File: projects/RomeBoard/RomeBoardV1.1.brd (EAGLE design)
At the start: 110 x 135 mm, 27 parts, among them J1 HEADER-5, J2 RASPBERRY-PI-HEADER, M1 2N7000, M2 2N7000, M3 2N7000, U1 LM1084IT-ADJ

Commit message: fixing air wire + updating library
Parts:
- M1, M2, M3: value 2N7000 -> ZVN4424A
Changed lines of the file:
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@@
 <element name="R6" library="passives" package="AXIAL-0.4" value="147R" x="5" y="46" rot="R270"/>
 <element name="R7" library="passives" package="AXIAL-0.4" value="147R" x="32" y="34" rot="R270"/>
-<element name="M1" library="BrownSpaceEngineering" package="TO-923-MOS" value="2N7000" x="26" y="63" rot="R270"/>
-<element name="M2" library="BrownSpaceEngineering" package="TO-923-MOS" value="2N7000" x="12" y="51" rot="R270"/>
-<element name="M3" library="BrownSpaceEngineering" package="TO-923-MOS" value="2N7000" x="26" y="39" rot="R270"/>
+<element name="M1" library="BrownSpaceEngineering" package="TO-923-MOS" value="ZVN4424A" x="26" y="63" rot="R270"/>
+<element name="M2" library="BrownSpaceEngineering" package="TO-923-MOS" value="ZVN4424A" x="12" y="51" rot="R270"/>
+<element name="M3" library="BrownSpaceEngineering" package="TO-923-MOS" value="ZVN4424A" x="26" y="39" rot="R270"/>
 <element name="R8" library="passives" package="AXIAL-0.4" value="10K" x="105" y="78" rot="R270"/>
 <element name="U1" library="BrownSpaceEngineering" package="TO-220-507302B00000G" value="LM1084IT-ADJ" x="80" y="11.5" smashed="yes" rot="R90">
@@
 <vertex x="51.5" y="6" curve="90"/>
 <vertex x="52" y="6.5"/>
-<vertex x="52" y="14.5" curve="-90"/>
-<vertex x="52.5" y="15"/>
-<vertex x="67.5" y="15" curve="-90"/>
-<vertex x="68" y="14.5"/>
-<vertex x="68" y="10.5" curve="90"/>
-<vertex x="68.5" y="10"/>
+<vertex x="52" y="15" curve="-90"/>
+<vertex x="52.5" y="15.5"/>
+<vertex x="67.5" y="15.5" curve="-90"/>
+<vertex x="68.5" y="15"/>
+<vertex x="68.5" y="10.5" curve="90"/>
+<vertex x="69" y="10"/>
 <vertex x="82.5" y="10" curve="90"/>
 <vertex x="83" y="10.5"/>
@@
 <polygon width="0.254" layer="1" isolate="0.3048" thermals="no">
 <vertex x="94.5" y="21.5"/>
-<vertex x="94.5" y="19.5" curve="-90"/>
-<vertex x="94" y="19"/>
+<vertex x="94.5" y="21" curve="-90"/>
+<vertex x="92.5" y="19"/>
 <vertex x="77" y="19" curve="90"/>
 <vertex x="76.5" y="18.5"/>
@@
 <vertex x="84" y="14" curve="-90"/>
 <vertex x="84.5" y="14.5"/>
-<vertex x="96" y="14.5" curve="-90"/>
-<vertex x="96.5" y="14"/>
-<vertex x="96.5" y="11" curve="90"/>
-<vertex x="97" y="10.5"/>
-<vertex x="104" y="10.5" curve="90"/>
-<vertex x="104.5" y="11"/>
-<vertex x="104.5" y="17" curve="90"/>
-<vertex x="104" y="17.5"/>
-<vertex x="102" y="17.5" curve="-90"/>
-<vertex x="101.5" y="18"/>
+<vertex x="94" y="14.5" curve="-90"/>
+<vertex x="96.5" y="12.5"/>
+<vertex x="96.5" y="12" curve="90"/>
+<vertex x="98" y="10.5"/>
+<vertex x="103" y="10.5" curve="90"/>
+<vertex x="104.5" y="12"/>
+<vertex x="104.5" y="16.5" curve="90"/>
+<vertex x="103.5" y="17.5" curve="-90"/>
+<vertex x="101.5" y="20"/>
 <vertex x="101.5" y="21" curve="90"/>
 <vertex x="101" y="21.5"/>

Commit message: for review
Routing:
- net 3V6: track 13.1 -> 16.5 mm
- net RX_L: track 71.5 -> 70.9 mm
- net GND: track 2.51 -> 2.91 mm, vias 106 -> 110
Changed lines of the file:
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@@
 <element name="U1" library="BrownSpaceEngineering" package="TO-220-507302B00000G" value="LM1084IT-ADJ" x="80" y="11.5" smashed="yes" rot="R90">
 <attribute name="NAME" x="81.31" y="17.14" size="1.27" layer="25" rot="R180"/>
-<attribute name="VALUE" x="76.94" y="7.93" size="1.27" layer="27" rot="R90"/>
+<attribute name="VALUE" x="76.57" y="3.94" size="1.27" layer="27" rot="R180"/>
 </element>
 <element name="R2" library="passives" package="AXIAL-0.4" value="450R" x="43" y="4.5"/>
@@
 <wire x1="39.36" y1="43.19" x2="39.36" y2="41.86" width="0.254" layer="1"/>
 <wire x1="39.36" y1="41.86" x2="39" y2="41.5" width="0.254" layer="1"/>
-<wire x1="39.2894" y1="45.7606" x2="39.36" y2="45.69" width="0.254" layer="1"/>
 <wire x1="35.5" y1="47" x2="35.5700125" y2="47" width="0.254" layer="1"/>
 <wire x1="44.06" y1="45.19" x2="44.06" y2="45.69" width="0.254" layer="1"/>
@@
 <contactref element="C1" pad="-"/>
 <contactref element="C3" pad="-"/>
-<wire x1="39.36" y1="45.69" x2="39.36" y2="45.19" width="0" layer="19" extent="1-1"/>
+<wire x1="39.36" y1="45.69" x2="39.36" y2="45.19" width="0.254" layer="1"/>
+<via x="42" y="49.5" extent="1-16" drill="0.35"/>
+<via x="41.5" y="48.5" extent="1-16" drill="0.35"/>
+<via x="42" y="47.5" extent="1-16" drill="0.35"/>
+<via x="41.5" y="46.5" extent="1-16" drill="0.35"/>
 </signal>
 <signal name="3V6">
@@
 <wire x1="80" y1="11.5" x2="84.42" y2="11.5" width="1.27" layer="1"/>
 <wire x1="84.42" y1="11.5" x2="86" y2="13.08" width="1.27" layer="1"/>
-<wire x1="40.64513125" y1="46" x2="41" y2="46" width="0.254" layer="1"/>
 <wire x1="39.36" y1="46.19" x2="39.383" y2="46.167" width="0.254" layer="1"/>
 <wire x1="39.383" y1="46.167" x2="40.47813125" y2="46.167" width="0.254" layer="1"/>
-<wire x1="40.47813125" y1="46.167" x2="40.64513125" y2="46" width="0.254" layer="1"/>
 <wire x1="41" y1="44.5" x2="39.67" y2="44.5" width="0.254" layer="1"/>
-<wire x1="39.67" y1="44.5" x2="39.36" y2="44.19" width="0.254" layer="1"/>
-<wire x1="41" y1="46" x2="41" y2="44.5" width="0.254" layer="1"/>
+<wire x1="39.67" y1="44.5" x2="39.585" y2="44.415" width="0.254" layer="1"/>
+<wire x1="39.585" y1="44.415" x2="39.36" y2="44.19" width="0.254" layer="1"/>
 <polygon width="0.254" layer="1" isolate="0.3048" thermals="no">
 <vertex x="82.5" y="12.5"/>
@@
 <vertex x="83" y="12" curve="90"/>
 </polygon>
+<wire x1="39.36" y1="46.19" x2="37.69" y2="46.19" width="0.254" layer="1"/>
+<wire x1="37.69" y1="46.19" x2="37.5" y2="46" width="0.254" layer="1"/>
+<wire x1="37.5" y1="46" x2="37.5" y2="44.5" width="0.254" layer="1"/>
+<wire x1="37.5" y1="44.5" x2="39.5" y2="44.5" width="0.254" layer="1"/>
+<wire x1="39.5" y1="44.5" x2="39.585" y2="44.415" width="0.254" layer="1"/>
 </signal>
 <signal name="VIN">
@@
 <vertex x="77" y="19" curve="90"/>
 <vertex x="76.5" y="18.5"/>
-<vertex x="76.5" y="14.5" curve="90"/>
-<vertex x="78" y="13"/>
+<vertex x="76.5" y="13.5" curve="90"/>
+<vertex x="77" y="13"/>
 <vertex x="83.5" y="13" curve="90"/>
 <vertex x="84" y="13.5"/>
@@
 <vertex x="101.5" y="21" curve="90"/>
 <vertex x="101" y="21.5"/>
-</polygon>
-<polygon width="0.254" layer="1" isolate="0.3048">
-<vertex x="78" y="13"/>
-<vertex x="77.5" y="19" curve="-90"/>
-<vertex x="78" y="18.5"/>
 </polygon>
 <polygon width="0.254" layer="16" isolate="0.3048" thermals="no">
@@
 <wire x1="39.36" y1="49.69" x2="13.31" y2="49.69" width="0.254" layer="1"/>
 <wire x1="13.31" y1="49.69" x2="12" y2="51" width="0.254" layer="1"/>
-<wire x1="39.36" y1="49.69" x2="39.4306" y2="49.7606" width="0.254" layer="1"/>
-<wire x1="39.4306" y1="49.7606" x2="40.52573125" y2="49.7606" width="0.254" layer="1"/>
-<wire x1="40.52573125" y1="49.7606" x2="40.6894" y2="49.92426875" width="0.254" layer="1"/>
-<wire x1="41.1806" y1="51.5106" x2="42.87573125" y2="51.5106" width="0.254" layer="1"/>
-<wire x1="40.6894" y1="51.0194" x2="41.1806" y2="51.5106" width="0.254" layer="1"/>
-<wire x1="40.6894" y1="49.92426875" x2="40.6894" y2="51.0194" width="0.254" layer="1"/>
-<wire x1="42.87573125" y1="51.5106" x2="47.5" y2="56.13486875" width="0.254" layer="1"/>
 <wire x1="61" y1="72.5" x2="62.1454" y2="73.6454" width="0.254" layer="16"/>
 <wire x1="63.39" y1="75.99013125" x2="63.39" y2="76.77" width="0.254" layer="16"/>
@@
 <wire x1="51" y1="71" x2="52.5" y2="72.5" width="0.254" layer="16"/>
 <wire x1="52.5" y1="72.5" x2="61" y2="72.5" width="0.254" layer="16"/>
+<wire x1="39.36" y1="49.69" x2="39.4306" y2="49.7606" width="0.254" layer="1"/>
+<wire x1="39.4306" y1="49.7606" x2="41.12573125" y2="49.7606" width="0.254" layer="1"/>
+<wire x1="41.12573125" y1="49.7606" x2="47.5" y2="56.13486875" width="0.254" layer="1"/>
 </signal>
 <signal name="PWR_L">

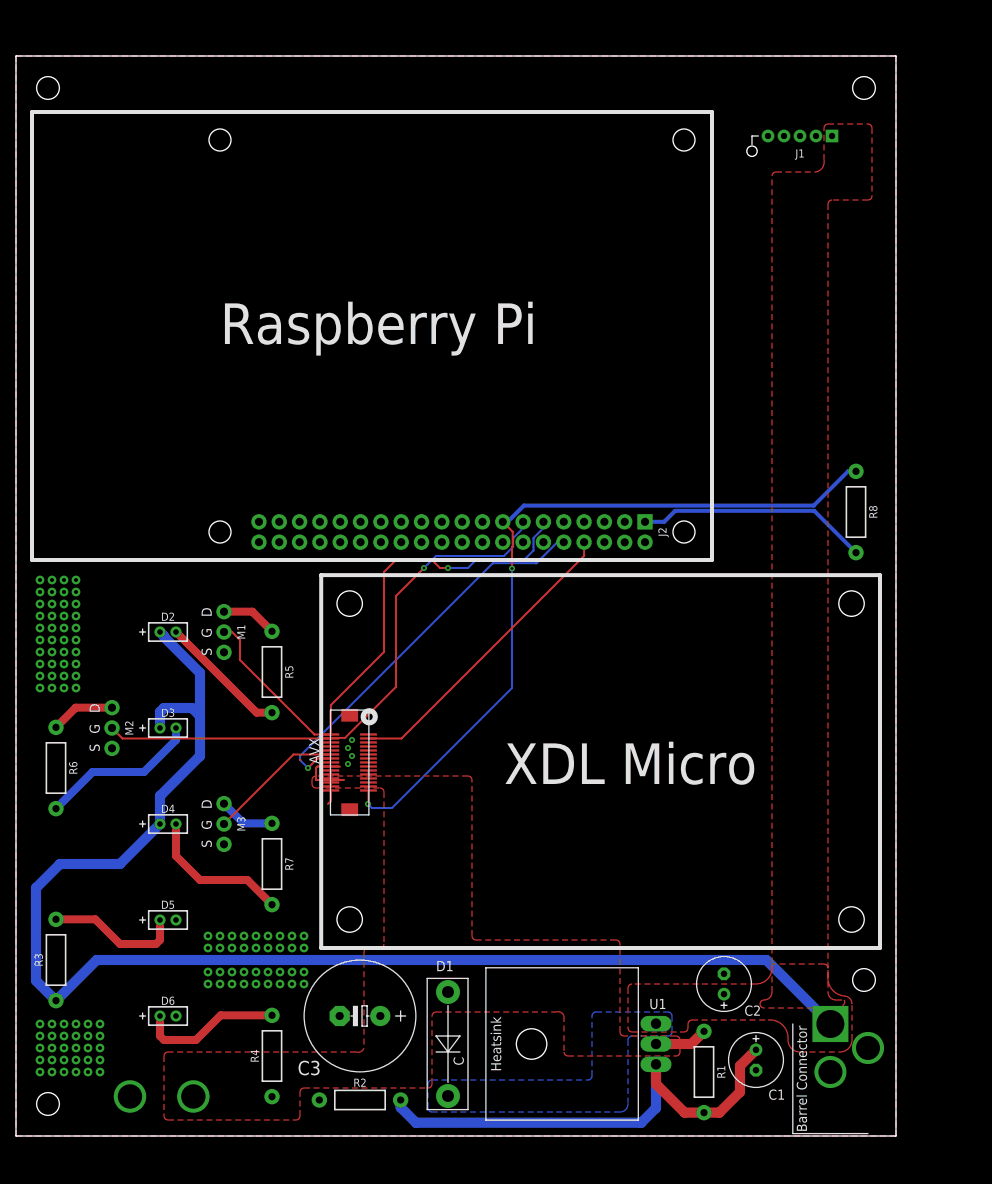
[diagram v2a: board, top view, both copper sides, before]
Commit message: Adding fan connectors to board, increasing board size, re-routing some stuff
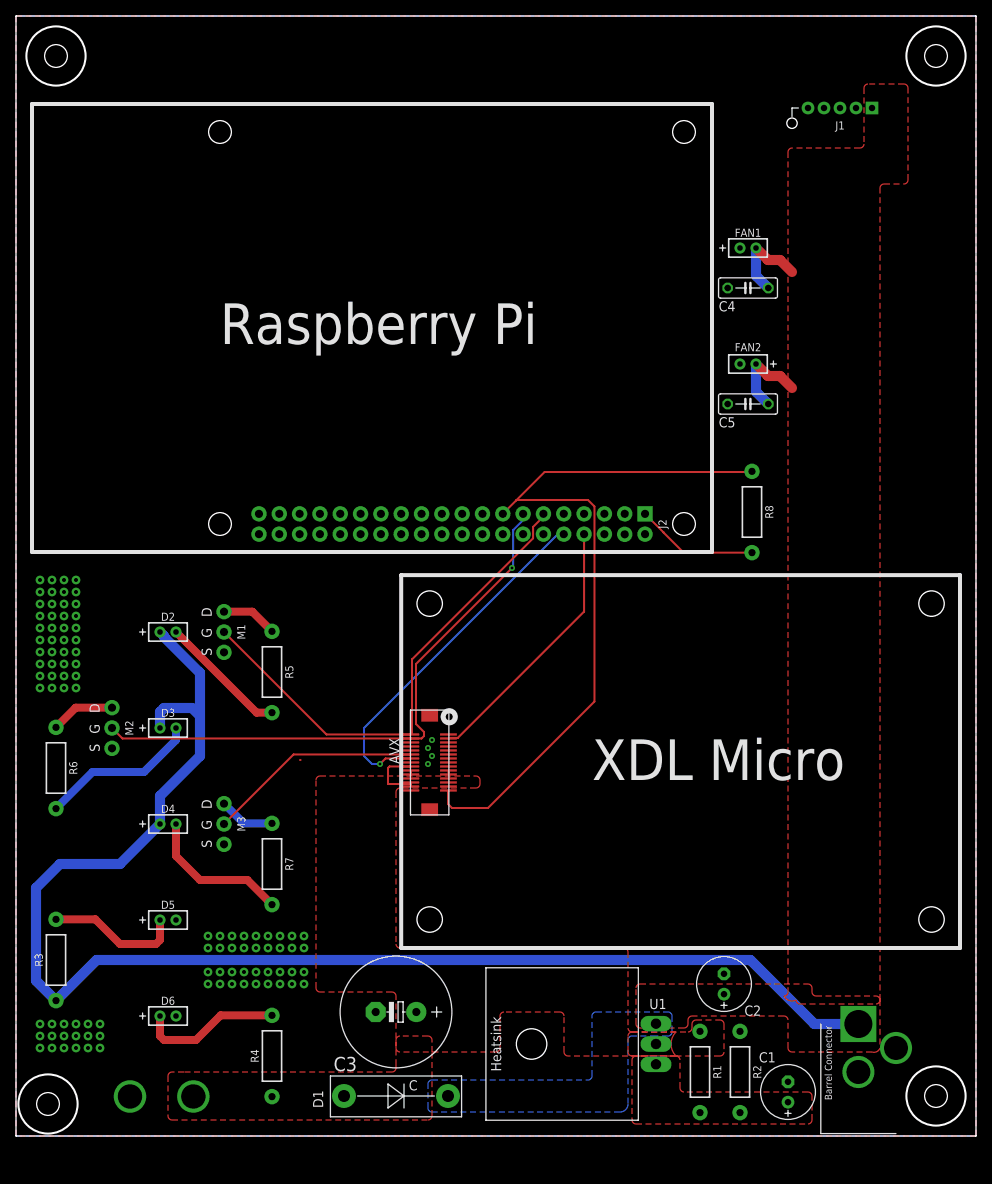
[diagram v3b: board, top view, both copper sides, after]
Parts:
- added C4, C5: 0.1uF, BrownSpaceEngineering:C050-025X075
- added FAN1, FAN2: FAD1-04010BBLW11, BrownSpaceEngineering:1X2-POL
- R2: value 450R -> 282R
- moved R2 47.6 mm to (90.5, 8.00), turned to 270 degrees
- moved R8 13.0 mm to (92.0, 78.0)
- moved AVX 10.0 mm to (51.7, 46.7)
- moved D1 9.19 mm to (47.5, 5.00), turned to 0 degrees
- moved J1 6.10 mm to (103.0, 128.5)
- moved C1 5.66 mm to (96.5, 5.50), turned to 90 degrees
- moved C3 4.53 mm to (47.5, 15.5)
- moved U$2 3.50 mm to (110.0, 11.0)
- moved J2 1.00 mm to (54.5, 76.5)
- moved R1 0.50 mm to (85.5, 8.00)
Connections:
- net GND: now also C4.2, C5.2, FAN1.1, FAN2.2
- net VIN: now also C4.1, C5.1, FAN1.2, FAN2.1
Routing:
- net N$8: track 61.5 -> 0.00 mm
- net VIN: track 171.9 -> 198.2 mm
- net 3V3: track 29.1 -> 15.4 mm
- net PWR_L: track 17.0 -> 27.0 mm
- net 3V6: track 16.5 -> 8.80 mm
- net TX_D: track 38.1 -> 33.2 mm
- net TX_L: track 67.9 -> 63.1 mm, vias 1 -> 0
- net RX_D: track 49.3 -> 45.1 mm
- net RX_L: track 70.9 -> 73.4 mm
- net GND: track 2.91 -> 1.07 mm, vias 110 -> 98
- net !SHDN: track 94.2 -> 93.5 mm, vias 2 -> 0
- added copper zone on layer 1, net N$8
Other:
- board size 110 x 135 mm -> 120 x 140 mm
- board text added: "5V in"
